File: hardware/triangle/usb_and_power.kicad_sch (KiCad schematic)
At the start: 16 parts, among them J1 USB_C_Receptacle_USB2.0_16P, J2 USB_C_Receptacle_USB2.0_16P, U2 EA8212HT6R

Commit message: triangel review
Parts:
- removed C25, C29: 47µF, Capacitor_SMD:C_1206_3216Metric, symbol Device:C
- removed R5, R6, R7, R8: 5.1kΩ, Resistor_SMD:R_0603_1608Metric, symbol Device:R_US
- added C30, C31, C33, C34: 10µF, Capacitor_SMD:C_0603_1608Metric, symbol Device:C
- added C32: 33nF, Capacitor_SMD:C_0402_1005Metric, symbol Device:C
- C26: value 100nF -> 33nF; LCSC Part # C1525 -> C507072
- L1: value MGFL2012F2R2MT-LF -> 4.7uH; footprint footprints:L0805 -> Inductor_SMD:L_Changjiang_FNR4030S; LCSC Part # C281115 -> C167874; MPN MGFL2012F2R2MT-LF -> FNR4030S4R7MT; Manufacturer microgate(麦捷科技) -> changjiang
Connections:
- net +12V: now also C30.1, C33.1, C34.1
- net +4V: now also C31.1, C32.2
- net GND: now also C30.2, C31.2, C33.2, C34.2
- net at R3.1, R4.1, U2.3 (FBK): now also C32.1
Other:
- moved on the sheet: C27, R3, R4

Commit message: updates to schematic based on feedback
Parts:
- removed C32: 33nF, Capacitor_SMD:C_0402_1005Metric, symbol Device:C
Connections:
- no-connect marks 0 -> 8
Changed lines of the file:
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@@
 	(paper "A4")
 	(junction
-		(at 57.15 170.18)
-		(diameter 0)
-		(color 0 0 0 0)
-	)
-	(junction
 		(at 198.12 44.45)
 		(diameter 0)
@@
 	)
 	(junction
-		(at 63.5 154.94)
-		(diameter 0)
-		(color 0 0 0 0)
-	)
-	(junction
 		(at 162.56 62.23)
 		(diameter 0)
 		(color 0 0 0 0)
 	)
+	(no_connect
+		(at 71.12 48.26)
+	)
+	(no_connect
+		(at 71.12 73.66)
+	)
+	(no_connect
+		(at 162.56 72.39)
+	)
+	(no_connect
+		(at 71.12 71.12)
+	)
+	(no_connect
+		(at 162.56 74.93)
+	)
+	(no_connect
+		(at 71.12 50.8)
+	)
+	(no_connect
+		(at 162.56 49.53)
+	)
+	(no_connect
+		(at 162.56 52.07)
+	)
 	(wire
 		(pts
@@
 	(wire
 		(pts
-			(xy 57.15 170.18) (xy 63.5 170.18)
-		)
-		(stroke
-			(width 0)
-			(type default)
-		)
-	)
-	(wire
-		(pts
-			(xy 48.26 170.18) (xy 57.15 170.18)
+			(xy 48.26 170.18) (xy 63.5 170.18)
 		)
 		(stroke
@@
 	(wire
 		(pts
-			(xy 63.5 128.905) (xy 63.5 154.94)
-		)
-		(stroke
-			(width 0)
-			(type default)
-		)
-	)
-	(wire
-		(pts
 			(xy 162.56 60.96) (xy 162.56 62.23)
 		)
@@
 	(wire
 		(pts
-			(xy 57.15 162.56) (xy 57.15 170.18)
-		)
-		(stroke
-			(width 0)
-			(type default)
-		)
-	)
-	(wire
-		(pts
 			(xy 127 128.27) (xy 127 133.35)
 		)
@@
 	(wire
 		(pts
-			(xy 57.15 154.94) (xy 63.5 154.94)
-		)
-		(stroke
-			(width 0)
-			(type default)
-		)
-	)
-	(wire
-		(pts
 			(xy 127 133.35) (xy 134.62 133.35)
 		)
@@
 	(wire
 		(pts
-			(xy 63.5 154.94) (xy 63.5 162.56)
+			(xy 63.5 128.905) (xy 63.5 162.56)
 		)
 		(stroke
@@
 					(unit 1)
 				)
-			)
-		)
-	)
-	(symbol
-		(lib_id "Device:C")
-		(at 57.15 158.75 180)
-		(unit 1)
-		(body_style 1)
-		(exclude_from_sim no)
-		(in_bom yes)
-		(on_board yes)
-		(in_pos_files yes)
-		(dnp yes)
-		(property "Reference" "C32"
-			(at 52.07 160.02 0)
-			(show_name no)
-			(do_not_autoplace no)
-			(effects
-				(font
-					(size 1.27 1.27)
-				)
-				(justify left)
-			)
-		)
-		(property "Value" "33nF"
-			(at 53.34 158.115 0)
-			(show_name no)
-			(do_not_autoplace no)
-			(effects
-				(font
-					(size 1.27 1.27)
-				)
-				(justify left)
-			)
-		)
-		(property "Footprint" "Capacitor_SMD:C_0402_1005Metric"
-			(at 56.1848 154.94 0)
-			(hide yes)
-			(show_name no)
-			(do_not_autoplace no)
-			(effects
-				(font
-					(size 1.27 1.27)
-				)
-			)
-		)
-		(property "Datasheet" "https://www.lcsc.com/datasheet/lcsc_datasheet_2304140030_Samsung-Electro-Mechanics-CL05B104KO5NNNC_C1525.pdf"
-			(at 57.15 158.75 0)
-			(hide yes)
-			(show_name no)
-			(do_not_autoplace no)
-			(effects
-				(font
-					(size 1.27 1.27)
-				)
-			)
-		)
-		(property "Description" "Unpolarized capacitor"
-			(at 57.15 158.75 0)
-			(hide yes)
-			(show_name no)
-			(do_not_autoplace no)
-			(effects
-				(font
-					(size 1.27 1.27)
-				)
-			)
-		)
-		(property "LCSC Part #" "C507072"
-			(at 57.15 158.75 0)
-			(hide yes)
-			(show_name no)
-			(do_not_autoplace no)
-			(effects
-				(font
-					(size 1.27 1.27)
-				)
-			)
-		)
-		(pin "2"
-		)
-		(pin "1"
-		)
-		(instances
-			(project "triangle"
-				(path "/955e9dc0-fcd6-4d32-9a7f-93a0bda4c269"
-					(reference "C32")
-					(unit 1)
-				)

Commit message: rearranging shared files and input board beginnings
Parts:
- J1, J2: footprint footprints:TYPE-C-SMD_USB4120-03-C -> easyeda2kicad:TYPE-C-SMD_USB4120-03-C
- U2: footprint footprints:SOT-23-6_L2.9-W1.6-P0.95-LS2.8-BR -> easyeda2kicad:SOT-23-6_L2.9-W1.6-P0.95-LS2.8-BR; symbol new:EA8212HT6R -> easyeda2kicad:EA8212HT6R
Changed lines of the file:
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@@
 			)
 		)
-		(property "Footprint" "footprints:TYPE-C-SMD_USB4120-03-C"
+		(property "Footprint" "easyeda2kicad:TYPE-C-SMD_USB4120-03-C"
 			(at 151.13 59.69 0)
 			(hide yes)
@@
 			)
 		)
-		(property "Footprint" "footprints:TYPE-C-SMD_USB4120-03-C"
+		(property "Footprint" "easyeda2kicad:TYPE-C-SMD_USB4120-03-C"
 			(at 59.69 58.42 0)
 			(hide yes)
@@
 	)
 	(symbol
-		(lib_id "new:EA8212HT6R")
+		(lib_id "easyeda2kicad:EA8212HT6R")
 		(at 89.535 152.4 0)
 		(unit 1)
@@
 			)
 		)
-		(property "Footprint" "footprints:SOT-23-6_L2.9-W1.6-P0.95-LS2.8-BR"
+		(property "Footprint" "easyeda2kicad:SOT-23-6_L2.9-W1.6-P0.95-LS2.8-BR"
 			(at 89.535 162.56 0)
 			(hide yes)

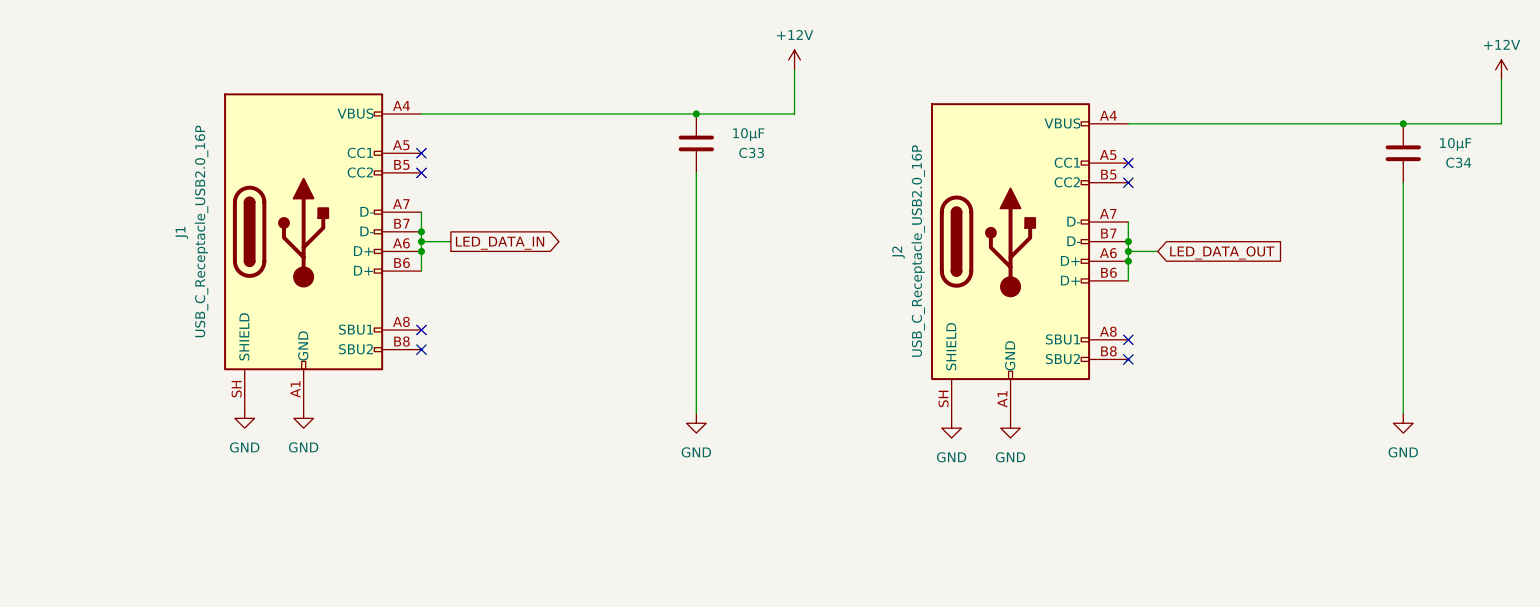
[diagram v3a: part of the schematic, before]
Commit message: triangle rework to use new symbols and get all shapes
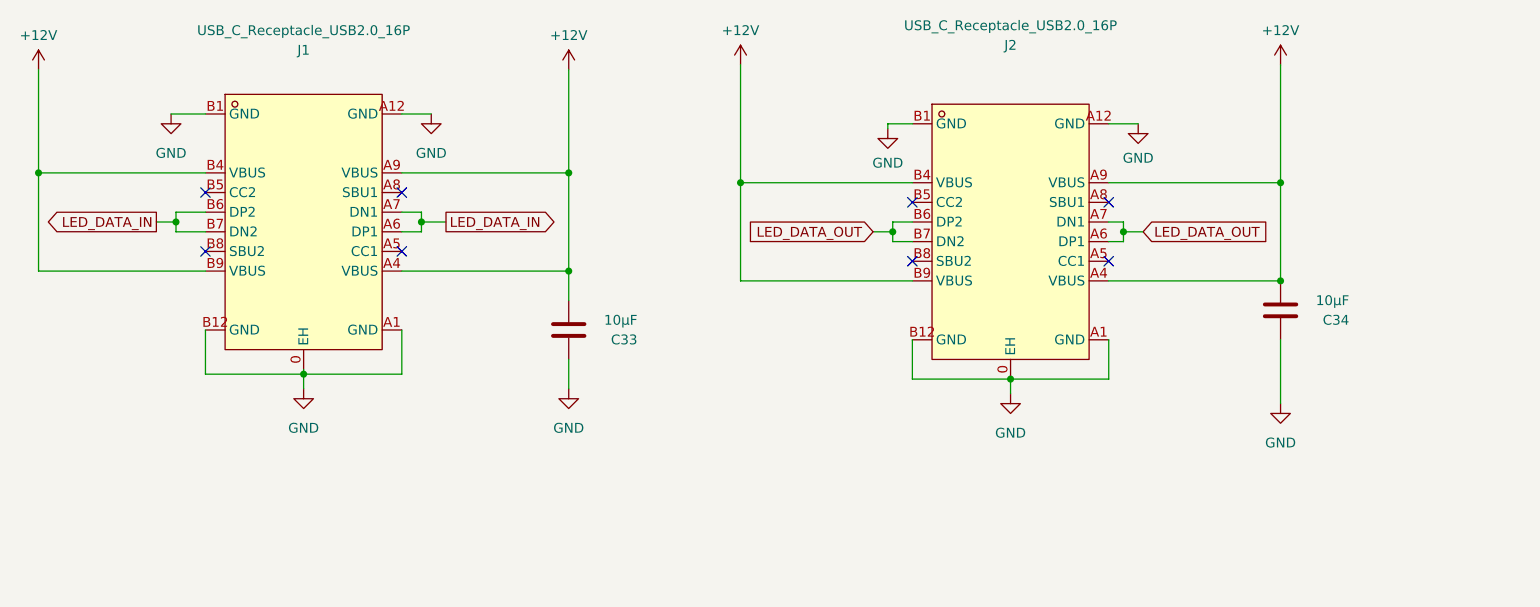
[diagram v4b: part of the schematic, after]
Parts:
- J1, J2: symbol Connector:USB_C_Receptacle_USB2.0_16P -> easyeda2kicad:TYPE-C16PLT-H10.0; LCSC Part (none) -> C3151749; MPN (none) -> TYPE-C 16PLT-H10.0; Manufacturer (none) -> SHOU HAN(首韩)
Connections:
- net GND: now also J1.0 (EH), J2.0 (EH); no longer J1.SH (SHIELD), J2.SH (SHIELD)
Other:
- moved on the sheet: C33, C34

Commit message: add ESD to triangles
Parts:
- added D25, D26: ESD8351XV2T1G_C19829478, easyeda2kicad:SOD-523_L1.2-W0.8-LS1.6-RD, symbol easyeda2kicad:ESD8351XV2T1G_C19829478
- added D27, D28: SMAJ15A_C19077535, easyeda2kicad:SMA_L4.3-W2.6-LS5.0-RD, symbol easyeda2kicad:SMAJ15A_C19077535
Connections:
- net +12V: now also D27.1 (K), D28.1 (K)
- net GND: now also D25.2 (A), D26.2 (A), D27.2 (A), D28.2 (A)
- net LED_DATA_IN: now also D25.1 (C)
- net LED_DATA_OUT: now also D26.1 (C)
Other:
- moved on the sheet: C34, J2
